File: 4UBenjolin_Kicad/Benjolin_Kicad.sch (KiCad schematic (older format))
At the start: 109 parts, among them J1 Conn_01x03_Female, J10 MAINOUT, J11 PWM, J12 RUN, J13 XOR, J14 CV_1, J15 CV_2, J2 Conn_02x05_Row_Letter_Last, J3 Conn_02x05_Row_Letter_Last, J4 EXT.INPUT, J5 CV_F, J6 PUL2, J7 TRI1, J8 TRI2, J9 PUL1, P10R1 10k, P11R1 10k, P1R1 10k, P2R1 10k, P3R1 10k, P4R1 10k, P5R1 10k, P6R1 10k, P8R1 10k, P9R1 10k, Q1 BC547, SW1 SW_SPDT, U1 TL074, U2 TL072, U3 TL074, U4 TL074, U5 SSI2164, U6 4021, U7 L78L09_SOT89

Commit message: Added footprints for banana PCB and made pcb size
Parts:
- removed J10: MAINOUT, Connector_Audio:Jack_3.5mm_QingPu_WQP-PJ398SM_Vertical_CircularHoles, symbol Connector:AudioJack2_Ground_Switch
- removed J11: PWM, Connector_Audio:Jack_3.5mm_QingPu_WQP-PJ398SM_Vertical_CircularHoles, symbol Connector:AudioJack2_Ground_Switch
- removed J12: RUN, Connector_Audio:Jack_3.5mm_QingPu_WQP-PJ398SM_Vertical_CircularHoles, symbol Connector:AudioJack2_Ground_Switch
- removed J13: XOR, Connector_Audio:Jack_3.5mm_QingPu_WQP-PJ398SM_Vertical_CircularHoles, symbol Connector:AudioJack2_Ground_Switch
- removed J14: CV_1, Connector_Audio:Jack_3.5mm_QingPu_WQP-PJ398SM_Vertical_CircularHoles, symbol Connector:AudioJack2_Ground_Switch
- removed J15: CV_2, Connector_Audio:Jack_3.5mm_QingPu_WQP-PJ398SM_Vertical_CircularHoles, symbol Connector:AudioJack2_Ground_Switch
- removed J4: EXT.INPUT, Connector_Audio:Jack_3.5mm_QingPu_WQP-PJ398SM_Vertical_CircularHoles, symbol Connector:AudioJack2_Ground_Switch
- removed J5: CV_F, Connector_Audio:Jack_3.5mm_QingPu_WQP-PJ398SM_Vertical_CircularHoles, symbol Connector:AudioJack2_Ground_Switch
- removed J6: PUL2, Connector_Audio:Jack_3.5mm_QingPu_WQP-PJ398SM_Vertical_CircularHoles, symbol Connector:AudioJack2_Ground_Switch
- removed J7: TRI1, Connector_Audio:Jack_3.5mm_QingPu_WQP-PJ398SM_Vertical_CircularHoles, symbol Connector:AudioJack2_Ground_Switch
- removed J8: TRI2, Connector_Audio:Jack_3.5mm_QingPu_WQP-PJ398SM_Vertical_CircularHoles, symbol Connector:AudioJack2_Ground_Switch
- removed J9: PUL1, Connector_Audio:Jack_3.5mm_QingPu_WQP-PJ398SM_Vertical_CircularHoles, symbol Connector:AudioJack2_Ground_Switch
- added J10: MAINOUT, SynthComponents:Banana_Jack_PCB, symbol Connector:Conn_01x01_Female
- added J11: PWM, SynthComponents:Banana_Jack_PCB, symbol Connector:Conn_01x01_Female
- added J12: RUN, SynthComponents:Banana_Jack_PCB, symbol Connector:Conn_01x01_Female
- added J13: XOR, SynthComponents:Banana_Jack_PCB, symbol Connector:Conn_01x01_Female
- added J14: CV_1, SynthComponents:Banana_Jack_PCB, symbol Connector:Conn_01x01_Female
- added J15: CV_2, SynthComponents:Banana_Jack_PCB, symbol Connector:Conn_01x01_Female
- added J4: EXT.INPUT, SynthComponents:Banana_Jack_PCB, symbol Connector:Conn_01x01_Female
- added J5: CV_F, SynthComponents:Banana_Jack_PCB, symbol Connector:Conn_01x01_Female
- added J6: PUL2, SynthComponents:Banana_Jack_PCB, symbol Connector:Conn_01x01_Female
- added J7: TRI1, SynthComponents:Banana_Jack_PCB, symbol Connector:Conn_01x01_Female
- added J8: TRI2, SynthComponents:Banana_Jack_PCB, symbol Connector:Conn_01x01_Female
- added J9: PUL1, SynthComponents:Banana_Jack_PCB, symbol Connector:Conn_01x01_Female
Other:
- moved on the sheet: J2, J3, P10R1, P11R1, P1R1, P2R1, P3R1, P4R1, P5R1, P6R1, P8R1, P9R1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

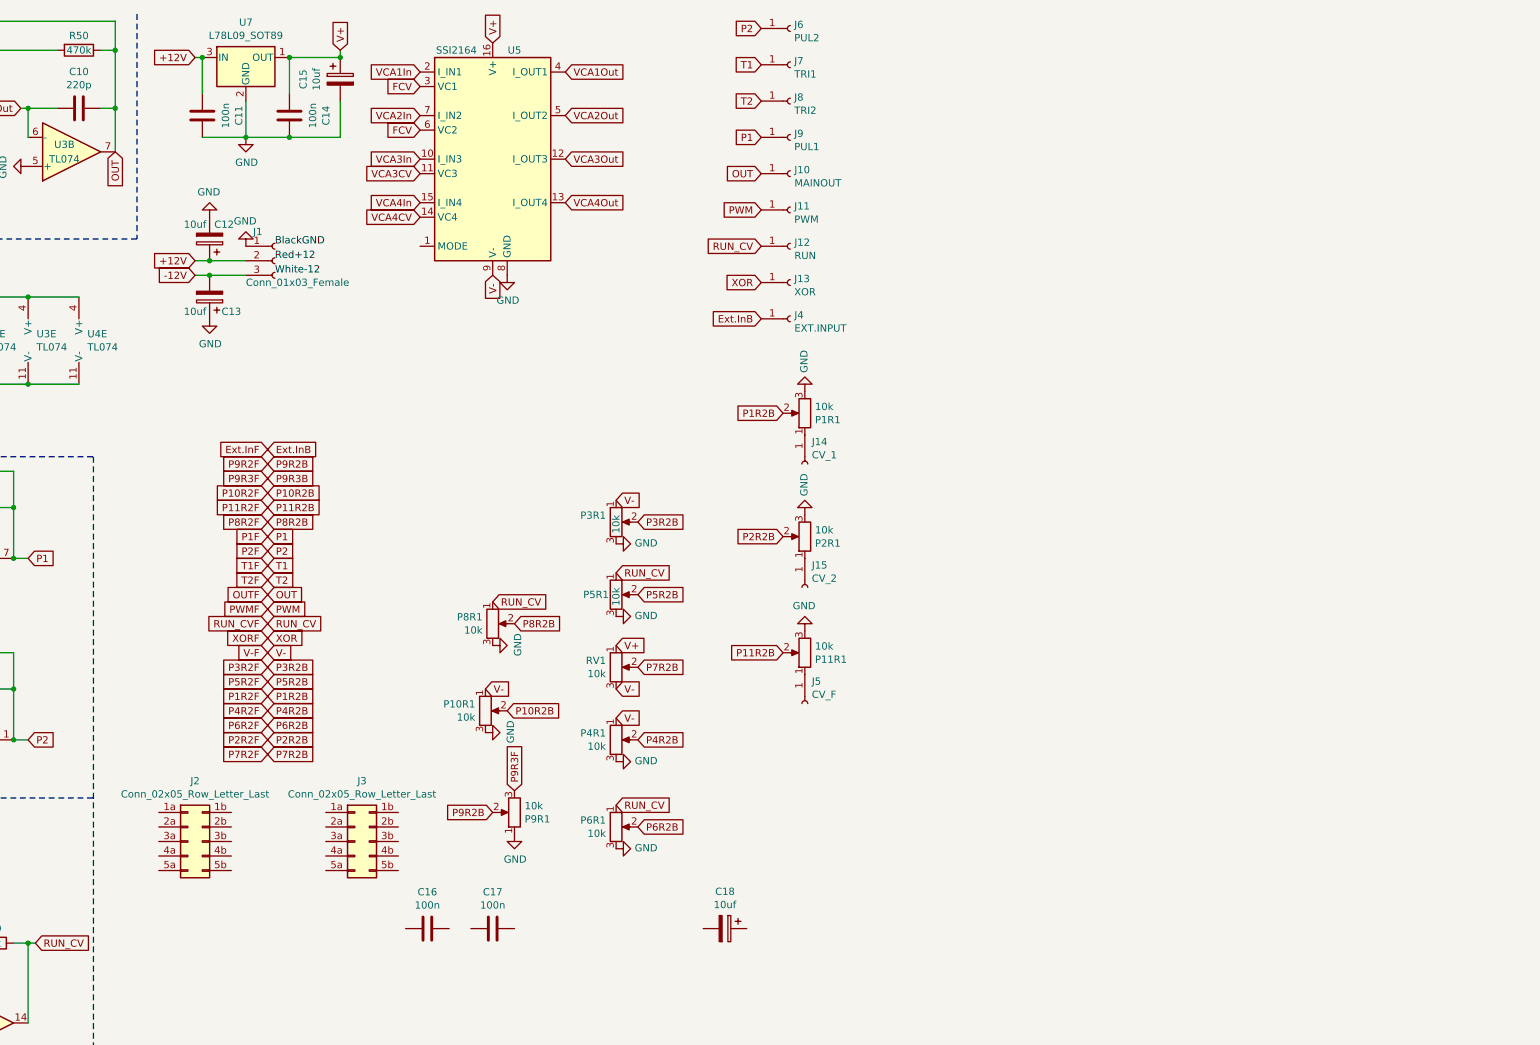
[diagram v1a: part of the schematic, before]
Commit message: Added footprints and symbols. added a mixer to the panel
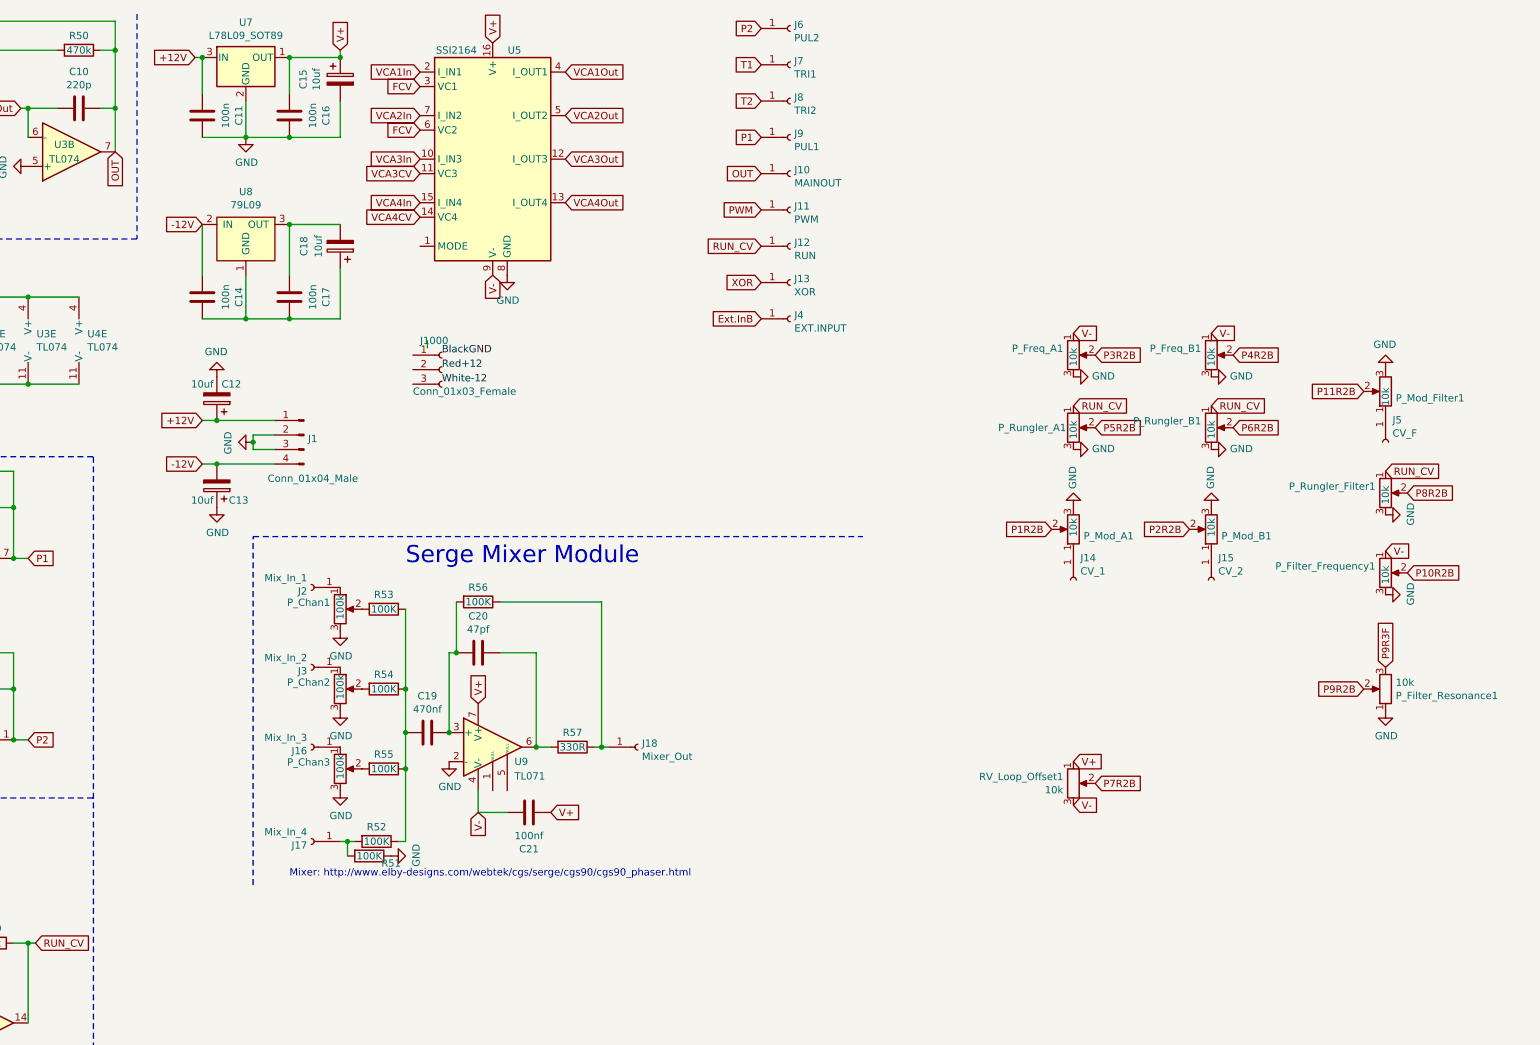
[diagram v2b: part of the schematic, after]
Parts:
- removed J2, J3: Conn_02x05_Row_Letter_Last, symbol Connector_Generic:Conn_02x05_Row_Letter_Last
- added C19: 470nf, Capacitor_THT:C_Disc_D8.0mm_W2.5mm_P5.00mm, symbol Device:C
- added C20: 47pf, Capacitor_THT:C_Disc_D8.0mm_W2.5mm_P5.00mm, symbol Device:C
- added C21: 100nf, Capacitor_THT:C_Disc_D8.0mm_W2.5mm_P5.00mm, symbol Device:C
- added J1: Conn_01x04_Male, Connector_Molex:Molex_Micro-Latch_53254-0470_1x04_P2.00mm_Horizontal, symbol Connector:Conn_01x04_Male
- added J16: Mix_In_3, SynthComponents:Banana_Jack_PCB, symbol Connector:Conn_01x01_Female
- added J17: Mix_In_4, SynthComponents:Banana_Jack_PCB, symbol Connector:Conn_01x01_Female
- added J18: Mixer_Out, SynthComponents:Banana_Jack_PCB, symbol Connector:Conn_01x01_Female
- added J2: Mix_In_1, SynthComponents:Banana_Jack_PCB, symbol Connector:Conn_01x01_Female
- added J3: Mix_In_2, SynthComponents:Banana_Jack_PCB, symbol Connector:Conn_01x01_Female
- added P_Chan1, P_Chan2, P_Chan3: 100k, SynthComponents:Potentiometer_Alps_RK09K_Single_Vertical, symbol Device:R_POT
- added R51, R52, R53, R54, R55, R56: 100K, Resistor_THT:R_Axial_DIN0204_L3.6mm_D1.6mm_P7.62mm_Horizontal, symbol Device:R
- added R57: 330R, Resistor_THT:R_Axial_DIN0204_L3.6mm_D1.6mm_P7.62mm_Horizontal, symbol Device:R
- added U8: 79L09, Package_TO_SOT_THT:TO-92L_Inline, symbol 79L09:79L09
- added U9: TL071, Package_DIP:DIP-8_W7.62mm_Socket_LongPads, symbol Amplifier_Operational:TL071
- C1, C10, C11, C14, C16, C17, C2, C3, C4, C5, C6, C7, C8, C9: footprint Capacitor_SMD:C_1206_3216Metric_Pad1.42x1.75mm_HandSolder -> Capacitor_THT:C_Disc_D8.0mm_W2.5mm_P5.00mm
- D1, D2, D3, D4, D5, D6: footprint Diode_THT:D_DO-35_SOD27_P2.54mm_Vertical_AnodeUp -> Diode_THT:D_A-405_P7.62mm_Horizontal
- P_Filter_Frequency1: renamed from P10R1; footprint Potentiometer_THT:Potentiometer_Alps_RK09K_Single_Vertical -> SynthComponents:Potentiometer_Alps_RK09K_Single_Vertical
- P_Filter_Resonance1: renamed from P9R1; footprint Potentiometer_THT:Potentiometer_Alps_RK09K_Single_Vertical -> SynthComponents:Potentiometer_Alps_RK09K_Single_Vertical
- P_Freq_A1: renamed from P3R1; footprint Potentiometer_THT:Potentiometer_Alps_RK09K_Single_Vertical -> SynthComponents:Potentiometer_Alps_RK09K_Single_Vertical
- P_Freq_B1: renamed from P4R1; footprint Potentiometer_THT:Potentiometer_Alps_RK09K_Single_Vertical -> SynthComponents:Potentiometer_Alps_RK09K_Single_Vertical
- P_Mod_A1: renamed from P1R1; footprint Potentiometer_THT:Potentiometer_Alps_RK09K_Single_Vertical -> SynthComponents:Potentiometer_Alps_RK09K_Single_Vertical
- P_Mod_B1: renamed from P2R1; footprint Potentiometer_THT:Potentiometer_Alps_RK09K_Single_Vertical -> SynthComponents:Potentiometer_Alps_RK09K_Single_Vertical
- P_Mod_Filter1: renamed from P11R1; footprint Potentiometer_THT:Potentiometer_Alps_RK09K_Single_Vertical -> SynthComponents:Potentiometer_Alps_RK09K_Single_Vertical
- P_Rungler_A1: renamed from P5R1; footprint Potentiometer_THT:Potentiometer_Alps_RK09K_Single_Vertical -> SynthComponents:Potentiometer_Alps_RK09K_Single_Vertical
- P_Rungler_B1: renamed from P6R1; footprint Potentiometer_THT:Potentiometer_Alps_RK09K_Single_Vertical -> SynthComponents:Potentiometer_Alps_RK09K_Single_Vertical
- P_Rungler_Filter1: renamed from P8R1; footprint Potentiometer_THT:Potentiometer_Alps_RK09K_Single_Vertical -> SynthComponents:Potentiometer_Alps_RK09K_Single_Vertical
- R1, R10, R11, R12, R13, R14, R15, R16, R17, R18, R19, R2, R20, R21, R22, R23, R24, R25, R26, R27, R28, R29, R3, R30, R31, R32, R33, R34, R35, R36, R37, R38, R39, R4, R40, R41, R42, R43, R44, R45, R46, R47, R48, R49, R5, R50, R6, R7, R8, R9: footprint Resistor_SMD:R_0603_1608Metric_Pad1.05x0.95mm_HandSolder -> Resistor_THT:R_Axial_DIN0204_L3.6mm_D1.6mm_P7.62mm_Horizontal
- RV_Loop_Offset1: renamed from RV1; footprint (none) -> SynthComponents:Potentiometer_Alps_RK09K_Single_Vertical
- U1, U3, U4: footprint Package_SO:SOIC-14_3.9x8.7mm_P1.27mm -> Package_DIP:DIP-14_W7.62mm_Socket_LongPads
- U2: footprint Package_SO:SOIC-8_3.9x4.9mm_P1.27mm -> Package_DIP:DIP-8_W7.62mm_Socket_LongPads
- U5, U6: footprint Package_SO:SOIC-16_3.9x9.9mm_P1.27mm -> Package_DIP:DIP-16_W7.62mm_Socket_LongPads
- renumbered J1 to J1000
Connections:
- net +12V: now also J1.1 (Pin_1); no longer J1000.2 (Pin_2)
- net -12V: now also C14.2, J1.4 (Pin_4), U8.2 (IN); no longer J1000.3 (Pin_3)
- net GND: now also C16.1, J1.2 (Pin_2), J1.3 (Pin_3), P_Chan1.3, P_Chan2.3, P_Chan3.3, R51.1, U9.2 (-); no longer C14.1, J1000.1 (Pin_1)
- net P9R3B: no longer P_Filter_Resonance1.3
- net V+: now also C16.2, C21.2, U9.7 (V+); no longer C14.2
- net V-: now also C21.1, U9.4 (V-)
- net at C17.1: now also C14.1, C18.1, U8.1 (GND)
- net at C17.2: now also C18.2, U8.3 (OUT)
- new net: C19.1, C20.2, R56.2, U9.3 (+)
- new net: C20.1, R57.2, U9.6
- new net: J2.1 (Pin_1), P_Chan1.1
- new net: P_Chan1.2, R53.2
- new net: J3.1 (Pin_1), P_Chan2.1
- new net: P_Chan2.2, R54.2
- new net: J16.1 (Pin_1), P_Chan3.1
- new net: P_Chan3.2, R55.2
- new net: J17.1 (Pin_1), R51.2, R52.2
- new net: J18.1 (Pin_1), R56.1, R57.1
- new net: C19.2, R52.1, R53.1, R54.1, R55.1
- new net P9R3F: P_Filter_Resonance1.3
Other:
- note added: "Mixer: http://www.elby-designs.com/webtek/cgs/serge/cgs90/cgs90_phaser.html"
- note added: "Serge Mixer Module"
- moved on the sheet: C12, C13, C14, C16, C17, C18, J1000, J14, J15, J5, P_Filter_Frequency1, P_Filter_Resonance1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

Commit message: traces complete
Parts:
- removed J1000: Conn_01x03_Female, Connector_PinSocket_2.54mm:PinSocket_1x03_P2.54mm_Vertical, symbol Connector:Conn_01x03_Female
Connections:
- net P9R3F is gone; now on net P9R3B: P_Filter_Resonance1.3
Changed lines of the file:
@@
 	5450 6900 5500 6900
 Connection ~ 5450 6900
-Text Label 8300 2950 0    50   ~ 0
-Red+12
-$Comp
-L Connector:Conn_01x03_Female J1000
-U 1 1 5C5E4D08
-P 8300 2950
-F 0 "J1000" H 8150 3150 50  0000 L CNN
-F 1 "Conn_01x03_Female" H 8100 2800 50  0000 L CNN
-F 2 "Connector_PinSocket_2.54mm:PinSocket_1x03_P2.54mm_Vertical" H 8300 2950 50  0001 C CNN
-F 3 "~" H 8300 2950 50  0001 C CNN
-	1    8300 2950
-	1    0    0    -1
-$EndComp
-Text Label 8300 2850 0    50   ~ 0
-BlackGND
-Text Label 8300 3050 0    50   ~ 0
-White-12
 Text GLabel 6650 3300 0    50   Input ~ 0
 +12V
@@
 Wire Wire Line
 	6750 3600 7150 3600
-Wire Wire Line
-	8200 2800 8200 2750
 $Comp
 L Device:R_POT P_Rungler_A1
@@
 P10R2B
 Text GLabel 14800 5000 1    50   Input ~ 0
-P9R3F
+P9R3B
 $Comp
 L power:GND #PWR0106
